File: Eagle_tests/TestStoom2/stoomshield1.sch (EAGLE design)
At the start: 35 parts, among them IC1 74HC245N

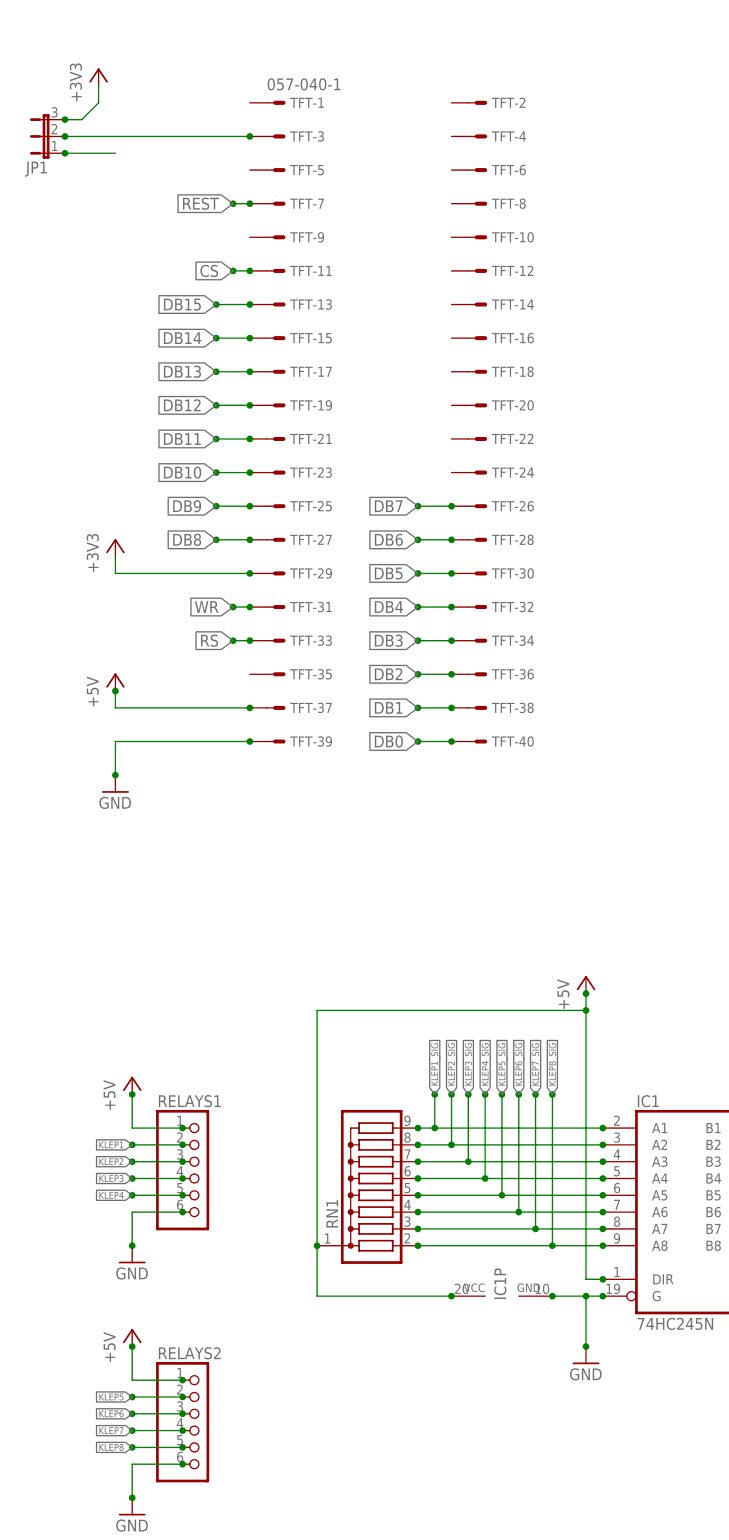
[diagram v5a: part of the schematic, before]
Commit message: Hardware test: improved eagle pcb+schema for relay.
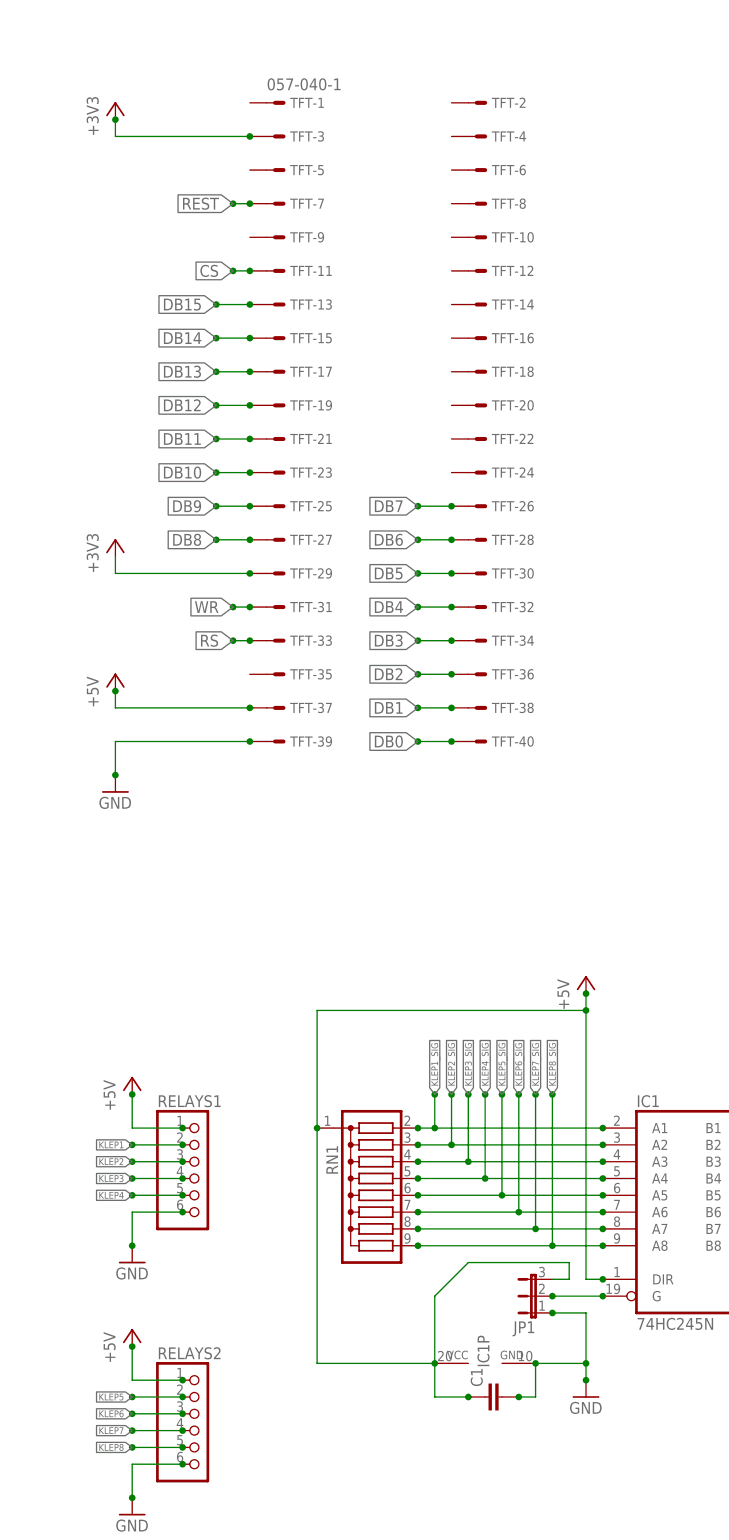
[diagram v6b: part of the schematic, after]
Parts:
- added C1: (no value), rcl:C-EU025-024X044
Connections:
- removed net N$2: JP1.1
- net +3V3: now also TFT-3.S; no longer JP1.3
- net +5V: now also C1.1, JP1.3
- net GND: now also C1.2, JP1.1; no longer IC1A.G
- net KLEP1_SIG: now also RN1.2; no longer RN1.9
- net KLEP2_SIG: now also RN1.3; no longer RN1.8
- net KLEP3_SIG: now also RN1.4; no longer RN1.7
- net KLEP4_SIG: now also RN1.5; no longer RN1.6
- net KLEP5_SIG: now also RN1.6; no longer RN1.5
- net KLEP6_SIG: now also RN1.7; no longer RN1.4
- net KLEP7_SIG: now also RN1.8; no longer RN1.3
- net KLEP8_SIG: now also RN1.9; no longer RN1.2
- net N$1: now also IC1A.G; no longer TFT-3.S
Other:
- moved on the sheet: IC1P, JP1, RN1
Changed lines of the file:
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@@
 <part name="GND2" library="supply1" deviceset="GND" device=""/>
 <part name="GND3" library="supply1" deviceset="GND" device=""/>
-<part name="JP1" library="jumper" deviceset="JP2E" device=""/>
 <part name="IC1" library="74xx-eu" deviceset="74*245" device="N" technology="HC"/>
 <part name="RELAYS1" library="pinhead" deviceset="PINHD-1X6" device=""/>
@@
 <part name="R14" library="resistor" deviceset="R-EU_" device="0204/5" value="1500"/>
 <part name="R15" library="resistor" deviceset="R-EU_" device="0204/5" value="1500"/>
+<part name="C1" library="rcl" deviceset="C-EU" device="025-024X044"/>
+<part name="JP1" library="jumper" deviceset="JP2E" device=""/>
 </parts>
 <sheets>
@@
 <instance part="GND2" gate="1" x="5.08" y="20.32"/>
 <instance part="GND3" gate="1" x="124.46" y="73.66"/>
-<instance part="JP1" gate="1" x="-5.08" y="119.38" rot="R90"/>
 <instance part="IC1" gate="A" x="91.44" y="-43.18"/>
 <instance part="RELAYS1" gate="A" x="17.78" y="-38.1"/>
 <instance part="RELAYS2" gate="A" x="17.78" y="-76.2"/>
-<instance part="GND4" gate="1" x="76.2" y="-66.04"/>
+<instance part="GND4" gate="1" x="76.2" y="-71.12"/>
 <instance part="GND5" gate="1" x="7.62" y="-88.9"/>
 <instance part="GND6" gate="1" x="7.62" y="-50.8"/>
-<instance part="RN1" gate="G$1" x="45.72" y="-38.1" rot="R90"/>
+<instance part="RN1" gate="G$1" x="45.72" y="-40.64" rot="MR270"/>
 <instance part="DUE_A" gate="A" x="142.24" y="-40.64"/>
-<instance part="IC1" gate="P" x="63.5" y="-55.88" rot="R90"/>
+<instance part="IC1" gate="P" x="60.96" y="-66.04" rot="R90"/>
 <instance part="OK1" gate="G$1" x="48.26" y="-149.86"/>
 <instance part="SENSOR1" gate="-1" x="15.24" y="-142.24"/>
@@
 <instance part="P+10" gate="1" x="5.08" y="38.1"/>
 <instance part="P+11" gate="1" x="124.46" y="137.16"/>
-<instance part="+3V1" gate="G$1" x="2.54" y="129.54"/>
+<instance part="+3V1" gate="G$1" x="5.08" y="124.46"/>
 <instance part="+3V2" gate="G$1" x="5.08" y="58.42"/>
 <instance part="GND8" gate="1" x="60.96" y="-353.06"/>
@@
 <instance part="R14" gate="G$1" x="30.48" y="-198.12"/>
 <instance part="R15" gate="G$1" x="30.48" y="-147.32"/>
+<instance part="C1" gate="G$1" x="60.96" y="-71.12" rot="R90"/>
+<instance part="JP1" gate="1" x="68.58" y="-55.88" rot="R90"/>
 </instances>
 <busses>
@@
 </segment>
 <segment>
-<pinref part="IC1" gate="A" pin="G"/>
 <pinref part="GND4" gate="1" pin="GND"/>
-<wire x1="78.74" y1="-55.88" x2="76.2" y2="-55.88" width="0.1524" layer="91"/>
-<wire x1="76.2" y1="-55.88" x2="76.2" y2="-63.5" width="0.1524" layer="91"/>
-<junction x="78.74" y="-55.88"/>
-<junction x="76.2" y="-63.5"/>
+<wire x1="76.2" y1="-66.04" x2="76.2" y2="-68.58" width="0.1524" layer="91"/>
+<junction x="76.2" y="-68.58"/>
 <pinref part="IC1" gate="P" pin="GND"/>
-<wire x1="76.2" y1="-55.88" x2="71.12" y2="-55.88" width="0.1524" layer="91"/>
-<junction x="71.12" y="-55.88"/>
-<junction x="76.2" y="-55.88"/>
+<wire x1="76.2" y1="-66.04" x2="68.58" y2="-66.04" width="0.1524" layer="91"/>
+<junction x="68.58" y="-66.04"/>
+<pinref part="C1" gate="G$1" pin="2"/>
+<wire x1="66.04" y1="-71.12" x2="68.58" y2="-71.12" width="0.1524" layer="91"/>
+<wire x1="68.58" y1="-71.12" x2="68.58" y2="-66.04" width="0.1524" layer="91"/>
+<junction x="66.04" y="-71.12"/>
+<pinref part="JP1" gate="1" pin="1"/>
+<wire x1="71.12" y1="-58.42" x2="76.2" y2="-58.42" width="0.1524" layer="91"/>
+<wire x1="76.2" y1="-58.42" x2="76.2" y2="-66.04" width="0.1524" layer="91"/>
+<junction x="71.12" y="-58.42"/>
+<junction x="76.2" y="-66.04"/>
 </segment>
 <segment>
@@
 </segment>
 </net>
-<net name="N$1" class="0">
-<segment>
-<pinref part="JP1" gate="1" pin="2"/>
-<pinref part="TFT" gate="-3" pin="S"/>
-<wire x1="-2.54" y1="119.38" x2="25.4" y2="119.38" width="0.1524" layer="91"/>
-<junction x="-2.54" y="119.38"/>
-<junction x="25.4" y="119.38"/>
-</segment>
-</net>
 <net name="KLEP1" class="0">
 <segment>
@@
 <junction x="78.74" y="-38.1"/>
 <junction x="60.96" y="-25.4"/>
-<pinref part="RN1" gate="G$1" pin="6"/>
+<pinref part="RN1" gate="G$1" pin="5"/>
 <wire x1="50.8" y1="-38.1" x2="60.96" y2="-38.1" width="0.1524" layer="91"/>
 <junction x="60.96" y="-38.1"/>
@@
 <junction x="78.74" y="-40.64"/>
 <junction x="63.5" y="-25.4"/>
-<pinref part="RN1" gate="G$1" pin="5"/>
+<pinref part="RN1" gate="G$1" pin="6"/>
 <wire x1="50.8" y1="-40.64" x2="63.5" y2="-40.64" width="0.1524" layer="91"/>
 <junction x="63.5" y="-40.64"/>
@@
 <junction x="78.74" y="-45.72"/>
 <junction x="68.58" y="-25.4"/>
-<pinref part="RN1" gate="G$1" pin="3"/>
+<pinref part="RN1" gate="G$1" pin="8"/>
 <wire x1="50.8" y1="-45.72" x2="68.58" y2="-45.72" width="0.1524" layer="91"/>
 <junction x="68.58" y="-45.72"/>
@@
 <junction x="78.74" y="-48.26"/>
 <junction x="71.12" y="-25.4"/>
-<pinref part="RN1" gate="G$1" pin="2"/>
+<pinref part="RN1" gate="G$1" pin="9"/>
 <wire x1="50.8" y1="-48.26" x2="71.12" y2="-48.26" width="0.1524" layer="91"/>
 <junction x="71.12" y="-48.26"/>
@@
 <junction x="78.74" y="-30.48"/>
 <junction x="53.34" y="-25.4"/>
-<pinref part="RN1" gate="G$1" pin="9"/>
+<pinref part="RN1" gate="G$1" pin="2"/>
 <wire x1="50.8" y1="-30.48" x2="53.34" y2="-30.48" width="0.1524" layer="91"/>
 <junction x="53.34" y="-30.48"/>
@@
 <junction x="78.74" y="-33.02"/>
 <junction x="55.88" y="-25.4"/>
-<pinref part="RN1" gate="G$1" pin="8"/>
+<pinref part="RN1" gate="G$1" pin="3"/>
 <wire x1="50.8" y1="-33.02" x2="55.88" y2="-33.02" width="0.1524" layer="91"/>
 <junction x="55.88" y="-33.02"/>
@@
 <junction x="78.74" y="-35.56"/>
 <junction x="58.42" y="-25.4"/>
-<pinref part="RN1" gate="G$1" pin="7"/>
+<pinref part="RN1" gate="G$1" pin="4"/>
 <wire x1="50.8" y1="-35.56" x2="58.42" y2="-35.56" width="0.1524" layer="91"/>
 <junction x="58.42" y="-35.56"/>
@@
 <junction x="78.74" y="-43.18"/>
 <junction x="66.04" y="-25.4"/>
-<pinref part="RN1" gate="G$1" pin="4"/>
+<pinref part="RN1" gate="G$1" pin="7"/>
 <wire x1="50.8" y1="-43.18" x2="66.04" y2="-43.18" width="0.1524" layer="91"/>
 <junction x="66.04" y="-43.18"/>
@@
 <junction x="132.08" y="-43.18"/>
 <junction x="139.7" y="-43.18"/>
-</segment>
-</net>
-<net name="N$2" class="0">
-<segment>
-<pinref part="JP1" gate="1" pin="1"/>
-<wire x1="5.08" y1="116.84" x2="-2.54" y2="116.84" width="0.1524" layer="91"/>
-<junction x="-2.54" y="116.84"/>
 </segment>
 </net>
@@
 <junction x="78.74" y="-53.34"/>
 <pinref part="RN1" gate="G$1" pin="1"/>
-<wire x1="35.56" y1="-48.26" x2="35.56" y2="-12.7" width="0.1524" layer="91"/>
+<wire x1="35.56" y1="-30.48" x2="35.56" y2="-12.7" width="0.1524" layer="91"/>
 <pinref part="IC1" gate="P" pin="VCC"/>
-<wire x1="55.88" y1="-55.88" x2="35.56" y2="-55.88" width="0.1524" layer="91"/>
-<wire x1="35.56" y1="-55.88" x2="35.56" y2="-48.26" width="0.1524" layer="91"/>
-<junction x="35.56" y="-48.26"/>
-<junction x="55.88" y="-55.88"/>
+<wire x1="53.34" y1="-66.04" x2="35.56" y2="-66.04" width="0.1524" layer="91"/>
+<wire x1="35.56" y1="-66.04" x2="35.56" y2="-30.48" width="0.1524" layer="91"/>
+<junction x="35.56" y="-30.48"/>
+<junction x="53.34" y="-66.04"/>
 <wire x1="35.56" y1="-12.7" x2="76.2" y2="-12.7" width="0.1524" layer="91"/>
 <junction x="76.2" y="-12.7"/>
 <pinref part="P+8" gate="1" pin="+5V"/>
 <junction x="76.2" y="-10.16"/>
+<pinref part="C1" gate="G$1" pin="1"/>
+<wire x1="58.42" y1="-71.12" x2="53.34" y2="-71.12" width="0.1524" layer="91"/>
+<wire x1="53.34" y1="-71.12" x2="53.34" y2="-66.04" width="0.1524" layer="91"/>
+<junction x="58.42" y="-71.12"/>
+<wire x1="53.34" y1="-55.88" x2="53.34" y2="-66.04" width="0.1524" layer="91"/>
+<pinref part="JP1" gate="1" pin="3"/>
+<wire x1="71.12" y1="-53.34" x2="73.66" y2="-53.34" width="0.1524" layer="91"/>
+<wire x1="73.66" y1="-53.34" x2="73.66" y2="-50.8" width="0.1524" layer="91"/>
+<wire x1="73.66" y1="-50.8" x2="58.42" y2="-50.8" width="0.1524" layer="91"/>
+<wire x1="53.34" y1="-55.88" x2="58.42" y2="-50.8" width="0.1524" layer="91"/>
 </segment>
 <segment>
@@
 <net name="+3V3" class="0">
 <segment>
-<wire x1="2.54" y1="127" x2="2.54" y2="124.46" width="0.1524" layer="91"/>
-<wire x1="2.54" y1="124.46" x2="0" y2="121.92" width="0.1524" layer="91"/>
-<pinref part="JP1" gate="1" pin="3"/>
-<wire x1="0" y1="121.92" x2="-2.54" y2="121.92" width="0.1524" layer="91"/>
-<junction x="-2.54" y="121.92"/>
+<wire x1="5.08" y1="121.92" x2="5.08" y2="119.38" width="0.1524" layer="91"/>
 <pinref part="+3V1" gate="G$1" pin="+3V3"/>
+<pinref part="TFT" gate="-3" pin="S"/>
+<wire x1="5.08" y1="119.38" x2="25.4" y2="119.38" width="0.1524" layer="91"/>
+<junction x="25.4" y="119.38"/>
+<junction x="5.08" y="121.92"/>
 </segment>
 <segment>
@@
 </segment>
 </net>
+<net name="N$1" class="0">
+<segment>
+<pinref part="IC1" gate="A" pin="G"/>
+<pinref part="JP1" gate="1" pin="2"/>
+<wire x1="78.74" y1="-55.88" x2="71.12" y2="-55.88" width="0.1524" layer="91"/>
+<junction x="71.12" y="-55.88"/>
+<junction x="78.74" y="-55.88"/>
+</segment>
+</net>

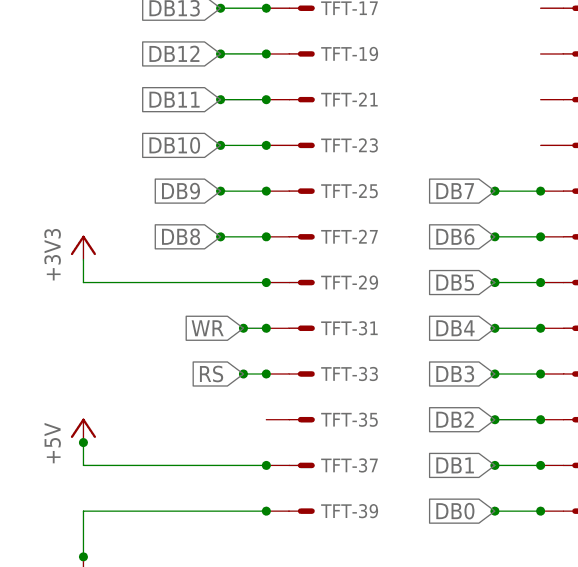
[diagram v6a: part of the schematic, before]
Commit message: Hardware schema: Fixed RS pull-up.
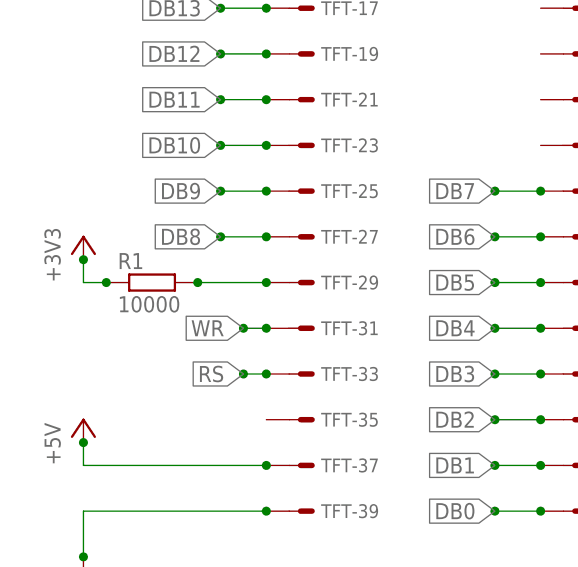
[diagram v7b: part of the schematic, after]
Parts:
- added R1: 10000, resistor:R-EU_0204/5
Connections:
- new net N$2: R1.2, TFT-29.S
- net +3V3: now also R1.1; no longer TFT-29.S
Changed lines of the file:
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@@
 <part name="C1" library="rcl" deviceset="C-EU" device="025-024X044"/>
 <part name="JP1" library="jumper" deviceset="JP2E" device=""/>
+<part name="R1" library="resistor" deviceset="R-EU_" device="0204/5" value="10000"/>
 </parts>
 <sheets>
@@
 <instance part="C1" gate="G$1" x="60.96" y="-71.12" rot="R90"/>
 <instance part="JP1" gate="1" x="68.58" y="-55.88" rot="R90"/>
+<instance part="R1" gate="G$1" x="12.7" y="53.34"/>
 </instances>
 <busses>
@@
 </segment>
 <segment>
-<pinref part="TFT" gate="-29" pin="S"/>
-<wire x1="25.4" y1="53.34" x2="5.08" y2="53.34" width="0.1524" layer="91"/>
+<pinref part="R1" gate="G$1" pin="1"/>
+<wire x1="7.62" y1="53.34" x2="5.08" y2="53.34" width="0.1524" layer="91"/>
+<pinref part="+3V2" gate="G$1" pin="+3V3"/>
 <wire x1="5.08" y1="53.34" x2="5.08" y2="55.88" width="0.1524" layer="91"/>
-<junction x="25.4" y="53.34"/>
-<pinref part="+3V2" gate="G$1" pin="+3V3"/>
+<junction x="5.08" y="55.88"/>
+<junction x="7.62" y="53.34"/>
 </segment>
 </net>
@@
 </segment>
 </net>
+<net name="N$2" class="0">
+<segment>
+<pinref part="R1" gate="G$1" pin="2"/>
+<pinref part="TFT" gate="-29" pin="S"/>
+<wire x1="17.78" y1="53.34" x2="25.4" y2="53.34" width="0.1524" layer="91"/>
+<junction x="17.78" y="53.34"/>
+<junction x="25.4" y="53.34"/>
+</segment>
+</net>
